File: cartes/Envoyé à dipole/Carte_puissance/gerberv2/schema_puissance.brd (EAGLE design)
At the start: 73.7 x 46.6 mm, 22 parts, among them X2 GMSTBA2

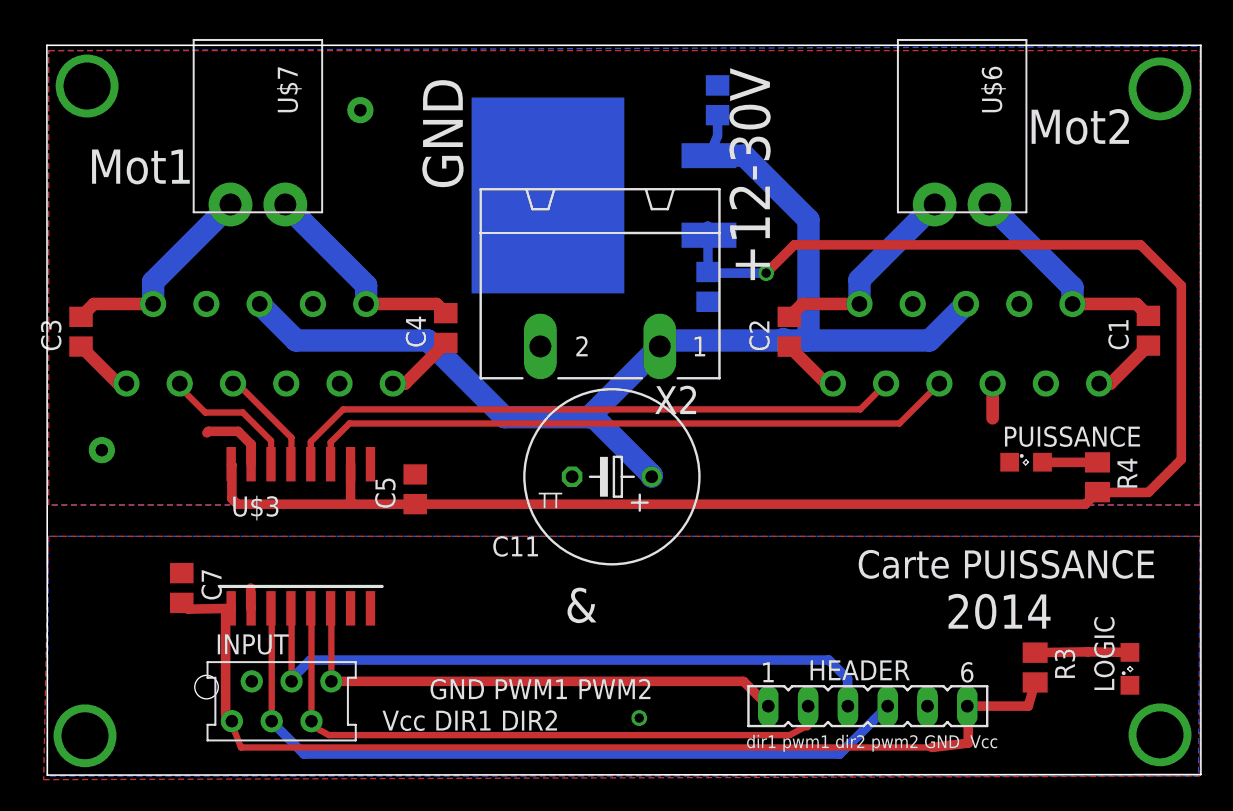
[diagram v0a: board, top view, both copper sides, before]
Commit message: ajout gerber puissance + export wiki
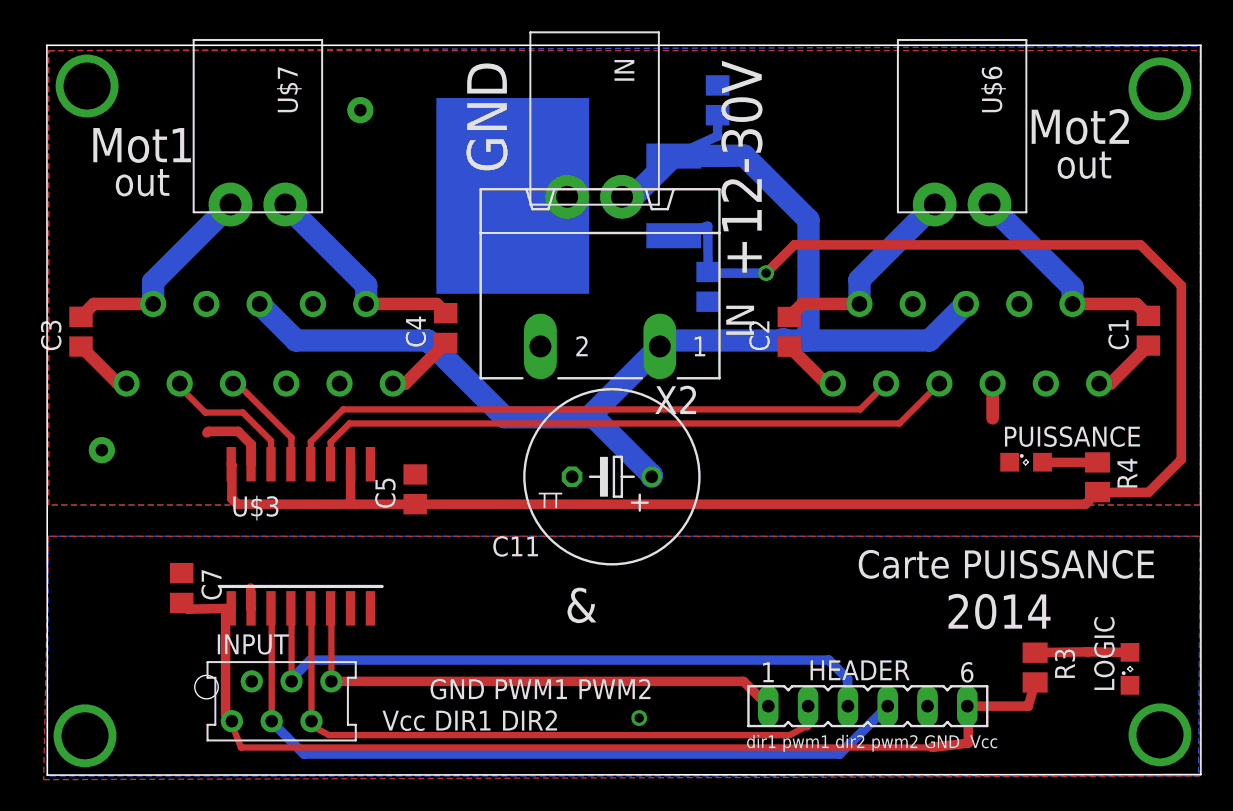
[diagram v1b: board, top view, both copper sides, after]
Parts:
- added IN: SL-3.5-2-90G, WEIDMULLER:SL-3.5-2-90G
- moved U$5 2.25 mm to (38.6, 43.7)
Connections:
- net +12V: now also IN.2
- net GNDA: now also IN.1
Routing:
- net +12V: track 75.3 -> 83.6 mm
- net +5V: track 113.4 -> 115.1 mm
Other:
- board text added: "IN"
- board text added: "out"
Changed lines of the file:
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@@
 <wire x1="82.55" y1="6.79" x2="82.55" y2="53.34" width="0.1" layer="20"/>
 <wire x1="82.55" y1="53.34" x2="8.89" y2="53.34" width="0.1" layer="20"/>
-<text x="11.5096" y="44.503840625" size="2.1844" layer="25" ratio="28" distance="58">Mot1</text>
+<text x="11.59088125" y="45.875440625" size="2.1844" layer="25" ratio="28" distance="58">Mot1</text>
 <text x="71.47808125" y="47.048240625" size="2.1844" layer="25" ratio="28" distance="58">Mot2</text>
 <text x="17.968959375" y="44.4632" size="2.1844" layer="26" ratio="28" distance="58" rot="MR0">Mot1</text>
@@
 <text x="30.3" y="9.6" size="1.27" layer="25" ratio="28" distance="58">      GND PWM1 PWM2
 Vcc DIR1 DIR2  </text>
-<text x="32.9" y="51.3" size="2.54" layer="25" ratio="28" distance="58" rot="R270">GND</text>
-<text x="52.5" y="51.9" size="2.54" layer="25" ratio="28" distance="58" rot="R270">+12-30V</text>
+<text x="35.714321875" y="52.3668" size="2.54" layer="25" ratio="28" distance="58" rot="R270">GND</text>
+<text x="51.981840625" y="52.37751875" size="2.54" layer="25" ratio="28" distance="58" rot="R270">+12-30V</text>
 <text x="79.7" y="21.1" size="1.778" layer="25" ratio="9" rot="R180">Carte PUISSANCE</text>
 <rectangle x1="48.925478125" y1="15.783565625" x2="48.955953125" y2="15.793721875" layer="200"/>
@@
 <text x="41.950640625" y="16.499840625" size="2.1844" layer="25" font="vector">&amp;</text>
 <text x="66.2432" y="16.1036" size="2.1844" layer="25" font="vector">2014</text>
+<text x="13.167359375" y="43.728640625" size="1.778" layer="25">out</text>
+<text x="73.28408125" y="44.846240625" size="1.778" layer="25">out</text>
+<text x="77.205840625" y="47.37608125" size="1.778" layer="26" rot="MR0">out</text>
+<text x="16.53031875" y="42.2656" size="1.778" layer="26" rot="MR0">out</text>
+<text x="54.03088125" y="34.6456" size="1.778" layer="25" rot="R90">IN</text>
 </plain>
 <attributes>
@@
 <element name="R3" library="rcl" package="M0805" value="1k" x="71.968959375" y="13.622959375" rot="R270"/>
 <element name="R4" library="rcl" package="M0805" value="1k" x="75.95" y="25.77" rot="R270"/>
-<element name="U$5" library="st-microelectronics" package="DPAK" value="L7805TO263" x="40.875" y="43.755" rot="MR270"/>
+<element name="U$5" library="st-microelectronics" package="DPAK" value="L7805TO263" x="38.629640625" y="43.724521875" rot="MR270"/>
 <element name="C9" library="rcl" package="C0805" value="100nF" x="51.1" y="37.92" rot="MR90"/>
 <element name="C10" library="rcl" package="C0805" value="330nF" x="51.7" y="49.83" rot="MR270"/>
@@
 <element name="C7" library="rcl" package="C0805" value="100nF" x="17.5" y="18.7" rot="R270"/>
 <element name="INPUT" library="jt-con-micromatch" package="AMP-215079-6" value="MMATCH-6-" x="20.7" y="10.2"/>
+<element name="IN" library="WEIDMULLER" package="SL-3.5-2-90G" value="SL-3.5-2-90G" x="43.850559375" y="43.667675" rot="R270"/>
 </elements>
 <signals>
@@
 <wire x1="21.1" y1="28.7" x2="19.2" y2="28.7" width="0.6096" layer="1"/>
 <wire x1="19.2" y1="28.7" x2="19.1" y2="28.6" width="0.6096" layer="1"/>
+<contactref element="IN" pad="1"/>
 </signal>
 <signal name="+12V">
@@
 <wire x1="56" y1="34.5" x2="48.39" y2="34.5" width="1.4224" layer="16"/>
 <wire x1="51.7" y1="48.88" x2="51.7" y2="47.545" width="0.6" layer="16"/>
-<wire x1="51.7" y1="47.545" x2="51.15" y2="46.295" width="0.6" layer="16"/>
+<wire x1="51.7" y1="47.545" x2="48.904640625" y2="46.264521875" width="0.6" layer="16"/>
 <contactref element="X2" pad="1"/>
 <wire x1="48.39" y1="34.5" x2="48.01" y2="34.12" width="1.4224" layer="16"/>
@@
 <wire x1="47.495" y1="25.905" x2="43.645" y2="29.755" width="1.4224" layer="16"/>
 <wire x1="55.9" y1="34.6" x2="56" y2="34.5" width="1.4224" layer="16"/>
-<wire x1="51.15" y1="46.295" x2="53.405" y2="46.295" width="1.4224" layer="16"/>
+<wire x1="48.904640625" y1="46.264521875" x2="53.405" y2="46.295" width="1.4224" layer="16"/>
 <wire x1="53.405" y1="46.295" x2="57.5" y2="42.2" width="1.4224" layer="16"/>
 <wire x1="57.5" y1="42.2" x2="57.5" y2="34.6" width="1.4224" layer="16"/>
 <wire x1="57.5" y1="34.6" x2="57.4" y2="34.5" width="1.4224" layer="16"/>
+<contactref element="IN" pad="2"/>
+<wire x1="45.600559375" y1="43.667675" x2="46.202584375" y2="43.667675" width="1.4224" layer="16"/>
+<wire x1="46.202584375" y1="43.667675" x2="46.3821875" y2="43.74206875" width="1.4224" layer="16" curve="44.999502"/>
+<wire x1="46.3821875" y1="43.74206875" x2="48.904640625" y2="46.264521875" width="1.4224" layer="16"/>
 </signal>
 <signal name="TF1">
@@
 <contactref element="R4" pad="2"/>
 <wire x1="51.1" y1="38.87" x2="51.07" y2="41.795" width="0.6" layer="16"/>
-<wire x1="51.07" y1="41.795" x2="51.15" y2="41.215" width="0.6" layer="16"/>
+<wire x1="51.07" y1="41.795" x2="48.904640625" y2="41.184521875" width="0.6" layer="16"/>
 <contactref element="U$3" pad="10"/>
 <contactref element="U$3" pad="16"/>
